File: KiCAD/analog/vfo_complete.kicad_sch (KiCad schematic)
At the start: 111 parts, among them J1 Filter Out, J10 Filter Out, J2 Filter Out, J3 Conn_01x02_Pin, J5 Conn_01x02_Pin, Q2 40673, Q3 2N3904, Q8 2N3904, U10 LM7171xIN, U11 LM7171xIN, U12 LM7171xIN, U13 LM7812_TO220, U14 LM317L_TO92, U21 LT1054, U22 LM7805_TO220, U5 Si5351A_Breakout, U9 MCP4921

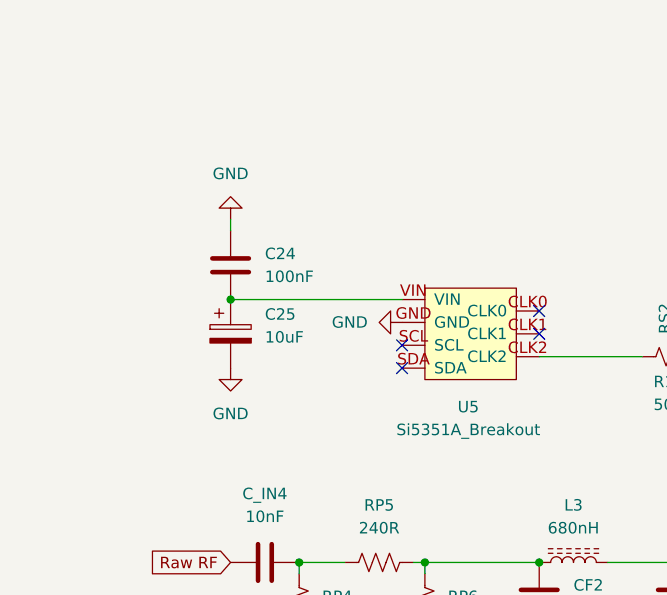
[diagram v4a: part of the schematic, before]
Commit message: KiCad revB: schematic review pass — I2C, ENC_INT, GND returns, GRID_BLOCK_CRASH clamp
Result of extended review pass against fresh netlists across all four
boards. All connectivity blockers resolved.

- Si5351 SDA/SCL wired via 0R jumpers (R8/R9) puts I2C on PCB traces
  for PCF8575 U17 and the RJ45 to the front panel. MCP4728 side has
  parallel 0R jumpers (R3/R4/R5) left DNP by default — STEMMA-QT is
  the intended path.
- ENC_INT chain unified end-to-end with staged names:
  ENC_INT_RAW (frontpanel encoder wire-OR) → ENC_INT_CLEAN (across
  CAT + analog pass-through) → ENC_INT_FINAL (post-protoshield
  conditioning). Frontpanel U4 (MCP1700-3.3 LDO) sources the +3.3V
  the pull-up R4 needs; pull-up moved to encoder side for sharper
  falling edges over the 2 m CAT run.
- Protoshield GRID_BLOCK_CRASH gets 1N4728A Zener clamp (D5),
  matching the I_CATHODE and MBL600 5V→3.3V clamp topology.
- Protoshield MBL600 conditioning rebuilt: 1K series + 100nF filter
  + 1N4728A clamp (was 10K/20K divider + 22pF that filtered nothing
  below RF).
- PADDLE_A/B and RESET_N removed from analog board — case-mounted
  switches wire directly to protoshield.
- Protoshield J1/J6 widened to 3-pin to include GND returns for the
  case-mounted paddle and reset switches.
- Bias board reference designators reorganized functionally
  (R_FA/R_FB feedback, R_GA/R_GB gain, R_PADA/R_PADB, R_GLA/R_GLB
  grid line, R_GATE, R_Z).
- New Documentation/control_board_functional_blocks.md captures
  KeyUp/Gate 2 keying, relay assignments (J6=T/R, J7=HV primary,
  J8=HV inrush), CD14538B heartbeat watchdog, TR_SENSE interlock,
  and J13 power-migration header.
- Fresh netlists exported for all four boards.

Co-Authored-By: Claude Opus 4.7 <noreply@anthropic.com>
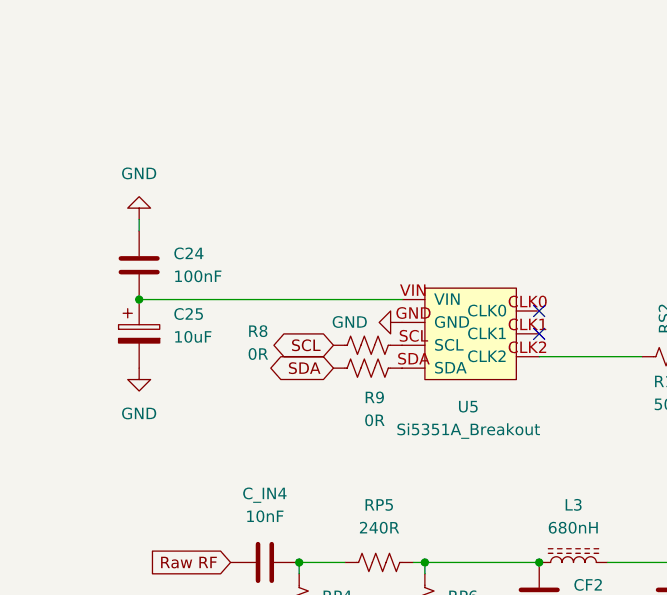
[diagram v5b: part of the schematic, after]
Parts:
- added R8, R9: 0R, symbol Device:R_US
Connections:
- net at U5.SCL: now also R8.2
- net at U5.SDA: now also R9.2
- new net SCL: R8.1
- new net SDA: R9.1
- no-connect marks 7 -> 5
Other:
- moved on the sheet: C24, C25

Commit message: KiCad revB: assign 87 empty footprints via re-runnable scripts
Filled empty Footprint fields on capacitors, resistors, and screw
terminals across all four boards. All three scripts are re-runnable
and only fill empty fields (never overwrite existing assignments).

Scripts:
- assign_cap_footprints.py: extended CAP_LIB_IDS to also cover
  Device:C_US, Device:C_Polarized_US, Device:C_Small (was only
  Device:C and Device:C_Polarized). VALUE_TO_FOOTPRINT map unchanged.
- assign_connector_footprints.py (new): matches
  Connector:Screw_Terminal_01xNN to Phoenix MKDS-1,5-N horizontal
  P5.00mm per pin count (same pattern the protoshield already used).
- assign_resistor_footprints.py (new): matches Device:R and
  Device:R_US to the project-standard Resistor_THT:R_Axial_DIN0207
  L6.3mm_D2.5mm_P10.16mm_Horizontal footprint. All 46 populated
  resistors on the project already used this footprint; the empty
  ones now match.

Assignment counts:
- Capacitors: 42 (5 arduino, 33 vfo_complete, 2 bias, 2 frontpanel)
- Screw terminals: 17 (10 arduino, 4 bias, 1 frontpanel, 2 protoshield)
- Resistors: 28 (5 arduino, 21 vfo_complete, 2 frontpanel)

Deferred (need part-specific decisions, tracked in review notes):
- Coax connectors (12 total across analog + bias) - awaiting Cinch
  142-0701-201 footprint verification in KiCad's Connector_Coaxial
  library, or a custom footprint in xmitter.pretty/
- One-off ICs: F1 Polyfuse, U3 MCP4728, U21 LT1054
- 6 unmapped cap values in vfo_complete: 2pF x3, 220nF, 4700uF, 100uF
- U2 Metro_ESP32S3 (protoshield): intentionally empty (on_board no,
  plug-in module, not placed on PCB)

Also add three component datasheets: 1N4736AT-D (1N4728A family
reference), LM393-D, OPA1641.

Co-Authored-By: Claude Opus 4.7 <noreply@anthropic.com>
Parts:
- C1, C2: footprint (none) -> Capacitor_THT:C_Rect_L7.0mm_W3.5mm_P5.00mm
- C26, C32, C56, C58, C60, C63, C64, C66, C68, C80, C88, C89: footprint (none) -> Capacitor_THT:C_Disc_D5.0mm_W2.5mm_P5.00mm
- C30, C31, C33, C57, C59, C61, C62, C65, C67, C81, C82, C84, C90: footprint (none) -> Capacitor_THT:CP_Radial_D5.0mm_P2.00mm
- C73, C74, C75, C76, C77, C78: footprint (none) -> Capacitor_THT:C_Disc_D6.0mm_W2.5mm_P5.00mm
- R1, R18, R2, R21, R22, R23, R24, R25, R31, R32, R33, R34, R35, R36, R37, R38, R39, R40, R41, R8, R9: footprint (none) -> Resistor_THT:R_Axial_DIN0207_L6.3mm_D2.5mm_P10.16mm_Horizontal
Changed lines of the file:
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@@
 			)
 		)
-		(property "Footprint" ""
+		(property "Footprint" "Capacitor_THT:C_Disc_D6.0mm_W2.5mm_P5.00mm"
 			(at 208.28 90.17 0)
 			(hide yes)
@@
 			)
 		)
-		(property "Footprint" ""
+		(property "Footprint" "Capacitor_THT:C_Disc_D5.0mm_W2.5mm_P5.00mm"
 			(at 200.66 151.13 0)
 			(hide yes)
@@
 			)
 		)
-		(property "Footprint" ""
+		(property "Footprint" "Resistor_THT:R_Axial_DIN0207_L6.3mm_D2.5mm_P10.16mm_Horizontal"
 			(at 164.084 101.854 90)
 			(hide yes)
@@
 			)
 		)
-		(property "Footprint" ""
+		(property "Footprint" "Resistor_THT:R_Axial_DIN0207_L6.3mm_D2.5mm_P10.16mm_Horizontal"
 			(at 101.346 54.864 90)
 			(hide yes)
@@
 			)
 		)
-		(property "Footprint" ""
+		(property "Footprint" "Resistor_THT:R_Axial_DIN0207_L6.3mm_D2.5mm_P10.16mm_Horizontal"
 			(at 181.864 75.184 90)
 			(hide yes)
@@
 			)
 		)
-		(property "Footprint" ""
+		(property "Footprint" "Capacitor_THT:CP_Radial_D5.0mm_P2.00mm"
 			(at 60.6552 162.56 0)
 			(hide yes)
@@
 			)
 		)
-		(property "Footprint" ""
+		(property "Footprint" "Resistor_THT:R_Axial_DIN0207_L6.3mm_D2.5mm_P10.16mm_Horizontal"
 			(at 51.054 51.054 90)
 			(hide yes)
@@
 			)
 		)
-		(property "Footprint" ""
+		(property "Footprint" "Resistor_THT:R_Axial_DIN0207_L6.3mm_D2.5mm_P10.16mm_Horizontal"
 			(at 227.076 145.034 90)
 			(hide yes)
@@
 			)
 		)
-		(property "Footprint" ""
+		(property "Footprint" "Capacitor_THT:C_Disc_D5.0mm_W2.5mm_P5.00mm"
 			(at 58.42 134.62 0)
 			(hide yes)
@@
 			)
 		)
-		(property "Footprint" ""
+		(property "Footprint" "Capacitor_THT:CP_Radial_D5.0mm_P2.00mm"
 			(at 194.31 128.27 0)
 			(hide yes)
@@
 			)
 		)
-		(property "Footprint" ""
+		(property "Footprint" "Resistor_THT:R_Axial_DIN0207_L6.3mm_D2.5mm_P10.16mm_Horizontal"
 			(at 228.854 35.814 90)
 			(hide yes)
@@
 			)
 		)
-		(property "Footprint" ""
+		(property "Footprint" "Capacitor_THT:C_Disc_D5.0mm_W2.5mm_P5.00mm"
 			(at 200.66 67.31 0)
 			(hide yes)
@@
 			)
 		)
-		(property "Footprint" ""
+		(property "Footprint" "Resistor_THT:R_Axial_DIN0207_L6.3mm_D2.5mm_P10.16mm_Horizontal"
 			(at 75.946 142.494 90)
 			(hide yes)
@@
 			)
 		)
-		(property "Footprint" ""
+		(property "Footprint" "Capacitor_THT:CP_Radial_D5.0mm_P2.00mm"
 			(at 241.3 25.4 0)
 			(hide yes)
@@
 			)
 		)
-		(property "Footprint" ""
+		(property "Footprint" "Capacitor_THT:C_Disc_D5.0mm_W2.5mm_P5.00mm"
 			(at 167.64 19.05 0)
 			(hide yes)
@@
 			)
 		)
-		(property "Footprint" ""
+		(property "Footprint" "Capacitor_THT:CP_Radial_D5.0mm_P2.00mm"
 			(at 194.31 151.13 0)
 			(hide yes)
@@
 			)
 		)
-		(property "Footprint" ""
+		(property "Footprint" "Capacitor_THT:C_Disc_D5.0mm_W2.5mm_P5.00mm"
 			(at 93.98 50.8 0)
 			(hide yes)
@@
 			)
 		)
-		(property "Footprint" ""
+		(property "Footprint" "Capacitor_THT:CP_Radial_D5.0mm_P2.00mm"
 			(at 194.31 90.17 0)
 			(hide yes)
@@
 			)
 		)
-		(property "Footprint" ""
+		(property "Footprint" "Resistor_THT:R_Axial_DIN0207_L6.3mm_D2.5mm_P10.16mm_Horizontal"
 			(at 108.966 42.164 90)
 			(hide yes)
@@
 			)
 		)
-		(property "Footprint" ""
+		(property "Footprint" "Capacitor_THT:CP_Radial_D5.0mm_P2.00mm"
 			(at 157.48 87.63 0)
 			(hide yes)
@@
 			)
 		)
-		(property "Footprint" ""
+		(property "Footprint" "Capacitor_THT:C_Disc_D5.0mm_W2.5mm_P5.00mm"
 			(at 163.83 64.77 0)
 			(hide yes)
@@
 			)
 		)
-		(property "Footprint" ""
+		(property "Footprint" "Resistor_THT:R_Axial_DIN0207_L6.3mm_D2.5mm_P10.16mm_Horizontal"
 			(at 51.054 48.514 90)
 			(hide yes)
@@
 			)
 		)
-		(property "Footprint" ""
+		(property "Footprint" "Capacitor_THT:CP_Radial_D5.0mm_P2.00mm"
 			(at 68.2752 146.05 0)
 			(hide yes)
@@
 			)
 		)
-		(property "Footprint" ""
+		(property "Footprint" "Capacitor_THT:C_Rect_L7.0mm_W3.5mm_P5.00mm"
 			(at 227.33 138.7348 0)
 			(hide yes)
@@
 			)
 		)
-		(property "Footprint" ""
+		(property "Footprint" "Capacitor_THT:CP_Radial_D5.0mm_P2.00mm"
 			(at 172.72 20.32 0)
 			(hide yes)
@@
 			)
 		)
-		(property "Footprint" ""
+		(property "Footprint" "Resistor_THT:R_Axial_DIN0207_L6.3mm_D2.5mm_P10.16mm_Horizontal"
 			(at 148.844 72.644 90)
 			(hide yes)
@@
 			)
 		)
-		(property "Footprint" ""
+		(property "Footprint" "Resistor_THT:R_Axial_DIN0207_L6.3mm_D2.5mm_P10.16mm_Horizontal"
 			(at 211.074 152.146 90)
 			(hide yes)
@@
 			)
 		)
-		(property "Footprint" ""
+		(property "Footprint" "Resistor_THT:R_Axial_DIN0207_L6.3mm_D2.5mm_P10.16mm_Horizontal"
 			(at 218.186 45.974 90)
 			(hide yes)
@@
 			)
 		)
-		(property "Footprint" ""
+		(property "Footprint" "Capacitor_THT:C_Disc_D6.0mm_W2.5mm_P5.00mm"
 			(at 187.96 67.31 0)
 			(hide yes)
@@
 			)
 		)
-		(property "Footprint" ""
+		(property "Footprint" "Capacitor_THT:C_Disc_D5.0mm_W2.5mm_P5.00mm"
 			(at 200.66 90.17 0)
 			(hide yes)
@@
 			)
 		)
-		(property "Footprint" ""
+		(property "Footprint" "Resistor_THT:R_Axial_DIN0207_L6.3mm_D2.5mm_P10.16mm_Horizontal"
 			(at 68.326 134.874 90)
 			(hide yes)
@@
 			)
 		)
-		(property "Footprint" ""
+		(property "Footprint" "Capacitor_THT:CP_Radial_D5.0mm_P2.00mm"
 			(at 194.31 67.31 0)
 			(hide yes)
@@
 			)
 		)
-		(property "Footprint" ""
+		(property "Footprint" "Resistor_THT:R_Axial_DIN0207_L6.3mm_D2.5mm_P10.16mm_Horizontal"
 			(at 89.916 54.864 90)
 			(hide yes)
@@
 			)
 		)
-		(property "Footprint" ""
+		(property "Footprint" "Capacitor_THT:C_Disc_D5.0mm_W2.5mm_P5.00mm"
 			(at 163.83 87.63 0)
 			(hide yes)
@@
 			)
 		)
-		(property "Footprint" ""
+		(property "Footprint" "Capacitor_THT:C_Disc_D5.0mm_W2.5mm_P5.00mm"
 			(at 252.73 24.13 0)
 			(hide yes)
@@
 			)
 		)
-		(property "Footprint" ""
+		(property "Footprint" "Capacitor_THT:C_Disc_D5.0mm_W2.5mm_P5.00mm"
 			(at 87.63 134.62 0)
 			(hide yes)
@@
 			)
 		)
-		(property "Footprint" ""
+		(property "Footprint" "Resistor_THT:R_Axial_DIN0207_L6.3mm_D2.5mm_P10.16mm_Horizontal"
 			(at 197.866 110.744 90)
 			(hide yes)
@@
 			)
 		)
-		(property "Footprint" ""
+		(property "Footprint" "Resistor_THT:R_Axial_DIN0207_L6.3mm_D2.5mm_P10.16mm_Horizontal"
 			(at 230.886 82.804 90)
 			(hide yes)
@@
 			)
 		)
-		(property "Footprint" ""
+		(property "Footprint" "Resistor_THT:R_Axial_DIN0207_L6.3mm_D2.5mm_P10.16mm_Horizontal"
 			(at 161.036 106.934 90)
 			(hide yes)
@@
 			)
 		)
-		(property "Footprint" ""
+		(property "Footprint" "Capacitor_THT:CP_Radial_D5.0mm_P2.00mm"
 			(at 115.2652 36.83 0)
 			(hide yes)
@@
 			)
 		)
-		(property "Footprint" ""
+		(property "Footprint" "Capacitor_THT:C_Disc_D5.0mm_W2.5mm_P5.00mm"
 			(at 200.66 128.27 0)
 			(hide yes)
@@
 			)
 		)
-		(property "Footprint" ""
+		(property "Footprint" "Capacitor_THT:C_Disc_D6.0mm_W2.5mm_P5.00mm"
 			(at 170.18 87.63 0)
 			(hide yes)
@@
 			)
 		)
-		(property "Footprint" ""
+		(property "Footprint" "Capacitor_THT:C_Disc_D6.0mm_W2.5mm_P5.00mm"
 			(at 187.96 128.27 0)
 			(hide yes)
@@
 			)
 		)
-		(property "Footprint" ""
+		(property "Footprint" "Capacitor_THT:CP_Radial_D5.0mm_P2.00mm"
 			(at 27.6352 143.51 0)
 			(hide yes)
@@
 			)
 		)
-		(property "Footprint" ""
+		(property "Footprint" "Resistor_THT:R_Axial_DIN0207_L6.3mm_D2.5mm_P10.16mm_Horizontal"
 			(at 211.074 40.894 90)
 			(hide yes)
@@
 			)
 		)
-		(property "Footprint" ""
+		(property "Footprint" "Capacitor_THT:CP_Radial_D5.0mm_P2.00mm"
 			(at 157.48 64.77 0)
 			(hide yes)
@@
 			)
 		)
-		(property "Footprint" ""
+		(property "Footprint" "Capacitor_THT:C_Disc_D5.0mm_W2.5mm_P5.00mm"
 			(at 67.31 158.75 0)
 			(hide yes)
@@
 			)
 		)
-		(property "Footprint" ""
+		(property "Footprint" "Capacitor_THT:C_Disc_D6.0mm_W2.5mm_P5.00mm"
 			(at 187.96 151.13 0)
 			(hide yes)
@@
 			)
 		)
-		(property "Footprint" ""
+		(property "Footprint" "Resistor_THT:R_Axial_DIN0207_L6.3mm_D2.5mm_P10.16mm_Horizontal"
 			(at 176.276 138.684 90)
 			(hide yes)
@@
 			)
 		)
-		(property "Footprint" ""
+		(property "Footprint" "Capacitor_THT:C_Rect_L7.0mm_W3.5mm_P5.00mm"
 			(at 229.87 77.7748 0)
 			(hide yes)
@@
 			)
 		)
-		(property "Footprint" ""
+		(property "Footprint" "Resistor_THT:R_Axial_DIN0207_L6.3mm_D2.5mm_P10.16mm_Horizontal"
 			(at 200.914 104.394 90)
 			(hide yes)
@@
 			)
 		)
-		(property "Footprint" ""
+		(property "Footprint" "Capacitor_THT:CP_Radial_D5.0mm_P2.00mm"
 			(at 53.0352 137.16 0)
 			(hide yes)
@@
 			)
 		)
-		(property "Footprint" ""
+		(property "Footprint" "Capacitor_THT:C_Disc_D6.0mm_W2.5mm_P5.00mm"
 			(at 170.18 64.77 0)
 			(hide yes)
@@
 			)
 		)
-		(property "Footprint" ""
+		(property "Footprint" "Resistor_THT:R_Axial_DIN0207_L6.3mm_D2.5mm_P10.16mm_Horizontal"
 			(at 233.426 33.274 90)
 			(hide yes)

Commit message: KiCad revB: custom footprints, coax assignments, TO-92 widening, ENC_INT rewire
Second-pass footprint work: filled the remaining empty footprints
that couldn't be handled by the earlier stock-library scripts, added
custom footprints for parts KiCad's stock library doesn't cover, and
did a few schematic hygiene fixes surfaced during the deep-dive
reviews.

Custom footprints (new, xmitter.pretty/):
- SMA_Cinch_142-0701-201_Vertical_JackPCB - 50 Ohm SMA vertical
  through-hole jack for the analog board and bias board coax
  interconnects (I_CATHODE, GRID_CTL, GRID_BLOCK_CRASH, GRID_BIAS).
  Center pin 1.57 mm hole + 4 ground tabs on a 5.08 mm square
  pattern. All 4 ground tabs share pin number 2 (shield).
- CP_Radial_Kemet_ESK_D22.0mm_P10.00mm - Kemet ESK case Q4 radial
  electrolytic (22 mm dia, 10 mm pitch) for C72 = 4700 uF 50V.
- Fuse_Littelfuse_60R_L7.9mm_W3.1mm_P5.08mm - Littelfuse 60R Series
  radial polyfuse for F1 = 60R050XU (0.5 A hold). Body sized for the
  small-body variants (010X-090X); pitch 5.08 mm, drill 0.7 mm.
- C_Axial_Kemet_Aximax_C41X_L4.5mm_D2.6mm_P7.62mm_Horizontal - Kemet
  Aximax C410 axial C0G ceramic for the three 2 pF caps
  (C69/C70/C71) in the vfo_complete keyer chain. Horizontal mount,
  7.62 mm pitch.

New re-runnable script:
- tools/assign_coax_footprints.py - maps
  Connector:Conn_Coaxial_Small symbols to the new Cinch SMA
  footprint. Same "only fill empty, never overwrite" pattern as the
  existing assign_*_footprints.py scripts.

Script extension:
- tools/assign_cap_footprints.py - added value entries for 4700uF
  (Kemet ESK), 220nF (D6 disc), 2pF (Kemet Aximax C41X), and 100uF
  (Vishay 036 RSP). All four entries include the datasheet path and
  the specific case-size rationale.

Schematic edits (all boards):
- 12 coax connectors assigned to the new Cinch SMA footprint
  (analog J17-J19/J23-J24, bias J1/J2/J4/J6/J9/J10/J12) via the new
  assign_coax script.
- 5 caps in vfo_complete assigned via extended assign_cap_footprints
  (C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
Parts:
- C69, C70, C71: footprint (none) -> xmitter:C_Axial_Kemet_Aximax_C41X_L4.5mm_D2.6mm_P7.62mm_Horizontal
- C72: footprint (none) -> xmitter:CP_Radial_Kemet_ESK_D22.0mm_P10.00mm
- C79: footprint (none) -> Capacitor_THT:C_Disc_D6.0mm_W2.5mm_P5.00mm
- C83: footprint (none) -> Capacitor_THT:CP_Radial_D8.0mm_P5.00mm
- U14: footprint Package_TO_SOT_THT:TO-92_Inline -> Package_TO_SOT_THT:TO-92_Inline_Wide
- U21: footprint (none) -> Package_DIP:DIP-8_W7.62mm
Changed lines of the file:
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@@
 			)
 		)
-		(property "Footprint" ""
+		(property "Footprint" "xmitter:C_Axial_Kemet_Aximax_C41X_L4.5mm_D2.6mm_P7.62mm_Horizontal"
 			(at 200.66 101.6 0)
 			(hide yes)
@@
 			)
 		)
-		(property "Footprint" ""
+		(property "Footprint" "Capacitor_THT:C_Disc_D6.0mm_W2.5mm_P5.00mm"
 			(at 88.9 158.75 0)
 			(hide yes)
@@
 			)
 		)
-		(property "Footprint" ""
+		(property "Footprint" "xmitter:C_Axial_Kemet_Aximax_C41X_L4.5mm_D2.6mm_P7.62mm_Horizontal"
 			(at 222.25 152.4 0)
 			(hide yes)
@@
 			)
 		)
-		(property "Footprint" ""
+		(property "Footprint" "xmitter:CP_Radial_Kemet_ESK_D22.0mm_P10.00mm"
 			(at 84.7852 180.34 0)
 			(hide yes)
@@
 			)
 		)
-		(property "Footprint" ""
+		(property "Footprint" "Capacitor_THT:CP_Radial_D8.0mm_P5.00mm"
 			(at 20.6248 129.54 0)
 			(hide yes)
@@
 			)
 		)
-		(property "Footprint" ""
+		(property "Footprint" "xmitter:C_Axial_Kemet_Aximax_C41X_L4.5mm_D2.6mm_P7.62mm_Horizontal"
 			(at 163.83 96.52 0)
 			(hide yes)
@@
 			)
 		)
-		(property "Footprint" ""
+		(property "Footprint" "Package_DIP:DIP-8_W7.62mm"
 			(at 35.56 139.7 0)
 			(hide yes)
@@
 			)
 		)
-		(property "Footprint" "Package_TO_SOT_THT:TO-92_Inline"
+		(property "Footprint" "Package_TO_SOT_THT:TO-92_Inline_Wide"
 			(at 74.93 125.095 0)
 			(hide yes)

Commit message: KiCad revB: add C8 phase-trim cap across R35 (LM7171 non-inv); add reference datasheets
C8: variable ceramic trimmer (1.5-5 pF, Vishay BFC2 808 20508) in
parallel with R35 in the U11 non-inverting op-amp feedback network,
to compensate the inv-vs-non-inv path phase mismatch of the LM7171
PP output at 14 MHz. Footprint assignment pending — separate commit.

References added:
- AN-762 Linear Amplifiers for Mobile Operation (Motorola)
- BFC2 808 5mm trimmer datasheet (Vishay, C8 part)
- QRP Labs 5W and 50W PA assembly manuals for SS output stage reference
- Bourns 3296 trimpot datasheet
- KEMET 22250A ceramic cap datasheet

Co-Authored-By: Claude Opus 4.7 <noreply@anthropic.com>
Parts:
- added C8: 1.5pF-5pF, symbol Device:C_Trim
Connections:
- net at C2.1, R35.2, TP3.1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: now also C8.2; no longer C70.2
- new net: C70.2, C8.1
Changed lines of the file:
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@@
 	)
 	(junction
+		(at 212.09 105.41)
+		(diameter 0)
+		(color 0 0 0 0)
+	)
+	(junction
 		(at 232.41 36.83)
 		(diameter 0)
@@
 	)
 	(junction
-		(at 204.47 105.41)
-		(diameter 0)
-		(color 0 0 0 0)
-	)
-	(junction
 		(at 232.41 21.59)
 		(diameter 0)
@@
 	(wire
 		(pts
-			(xy 204.47 101.6) (xy 204.47 105.41)
-		)
-		(stroke
-			(width 0)
-			(type default)
-		)
-	)
-	(wire
-		(pts
 			(xy 187.96 154.94) (xy 194.31 154.94)
 		)
@@
 	(wire
 		(pts
+			(xy 212.09 105.41) (xy 218.44 105.41)
+		)
+		(stroke
+			(width 0)
+			(type default)
+		)
+	)
+	(wire
+		(pts
 			(xy 83.82 130.81) (xy 83.82 154.94)
 		)
@@
 	(wire
 		(pts
-			(xy 204.47 105.41) (xy 218.44 105.41)
+			(xy 204.47 105.41) (xy 212.09 105.41)
 		)
 		(stroke
@@
 	(wire
 		(pts
+			(xy 212.09 101.6) (xy 212.09 105.41)
+		)
+		(stroke
+			(width 0)
+			(type default)
+		)
+	)
+	(wire
+		(pts
 			(xy 165.1 39.37) (xy 170.18 39.37)
 		)
@@
 					(unit 1)
 				)
+			)
+		)
+	)
+	(symbol
+		(lib_id "Device:C_Trim")
+		(at 208.28 101.6 90)
+		(unit 1)
+		(body_style 1)
+		(exclude_from_sim no)
+		(in_bom yes)
+		(on_board yes)
+		(in_pos_files yes)
+		(dnp no)
+		(property "Reference" "C8"
+			(at 209.55 108.712 90)
+			(show_name no)
+			(do_not_autoplace no)
+			(effects
+				(font
+					(size 1.27 1.27)
+				)
+			)
+		)
+		(property "Value" "1.5pF-5pF"
+			(at 208.026 96.52 90)
+			(show_name no)
+			(do_not_autoplace no)
+			(effects
+				(font
+					(size 1.27 1.27)
+				)
+			)
+		)
+		(property "Footprint" ""
+			(at 208.28 101.6 0)
+			(hide yes)
+			(show_name no)
+			(do_not_autoplace no)
+			(effects
+				(font
+					(size 1.27 1.27)
+				)
+			)
+		)
+		(property "Datasheet" ""
+			(at 208.28 101.6 0)
+			(hide yes)
+			(show_name no)
+			(do_not_autoplace no)
+			(effects
+				(font
+					(size 1.27 1.27)
+				)
+			)
+		)
+		(property "Description" "Trimmable capacitor"
+			(at 208.28 101.6 0)
+			(hide yes)
+			(show_name no)
+			(do_not_autoplace no)
+			(effects
+				(font
+					(size 1.27 1.27)
+				)
+			)
+		)
+		(pin "2"
+		)
+		(pin "1"
+		)
+		(instances
+			(project "analog"
+				(path "/d3de40b8-856b-4fbd-829c-f45ffcd55742/94bbc356-fa50-4d6f-b6f0-2ea7eca96dd3"
+					(reference "C8")
+					(unit 1)
+				)
